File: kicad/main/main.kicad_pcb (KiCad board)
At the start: 2 copper layers, 99.1 x 99.1 mm, 29 parts, among them J1 Barrel_Jack_MountingPin, SW1 Reset, SW2 SW_DIP_x08, U1 GAL16V8, U2 Z80CPU, U3 DS1813-5+, U4 AS6C4008-55PCN, U5 L7805, U6 74HC273, U7 27C512, U8 74HC244, X1 4 MHz

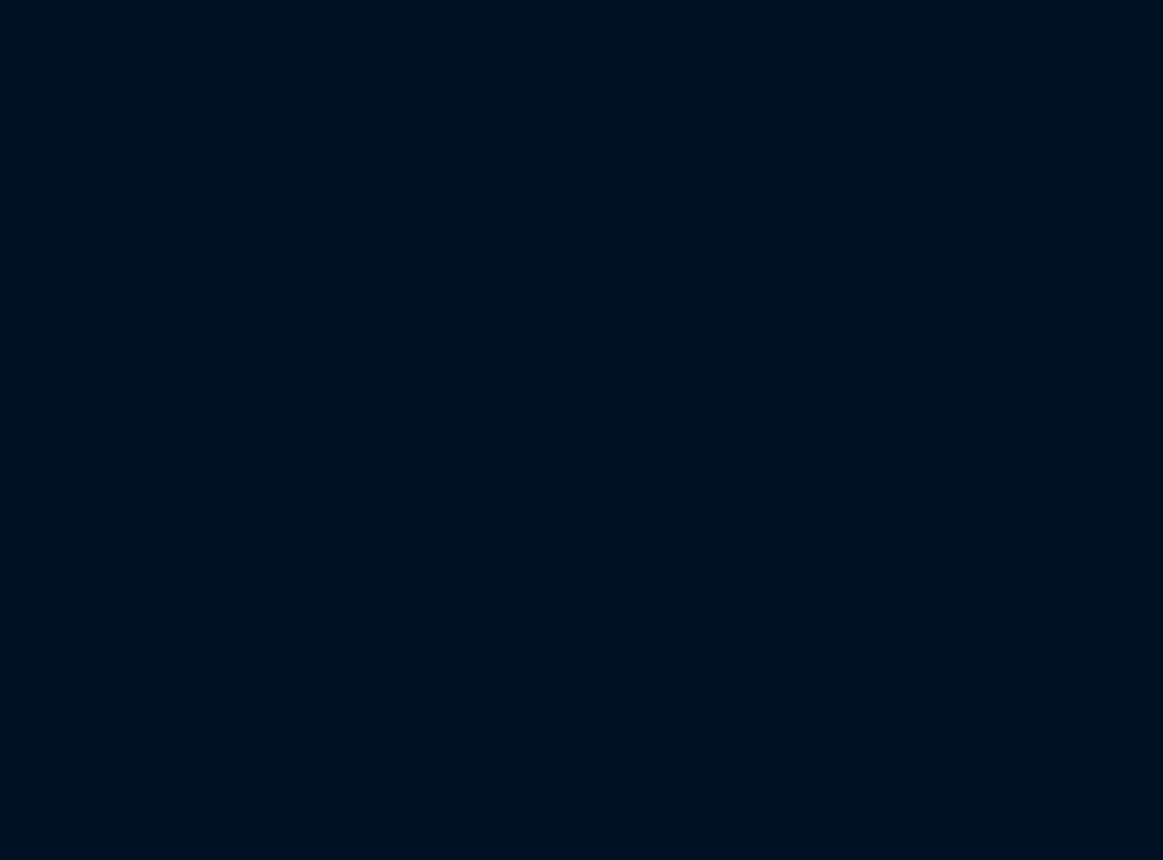
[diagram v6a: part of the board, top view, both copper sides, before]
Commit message: Add new buffers
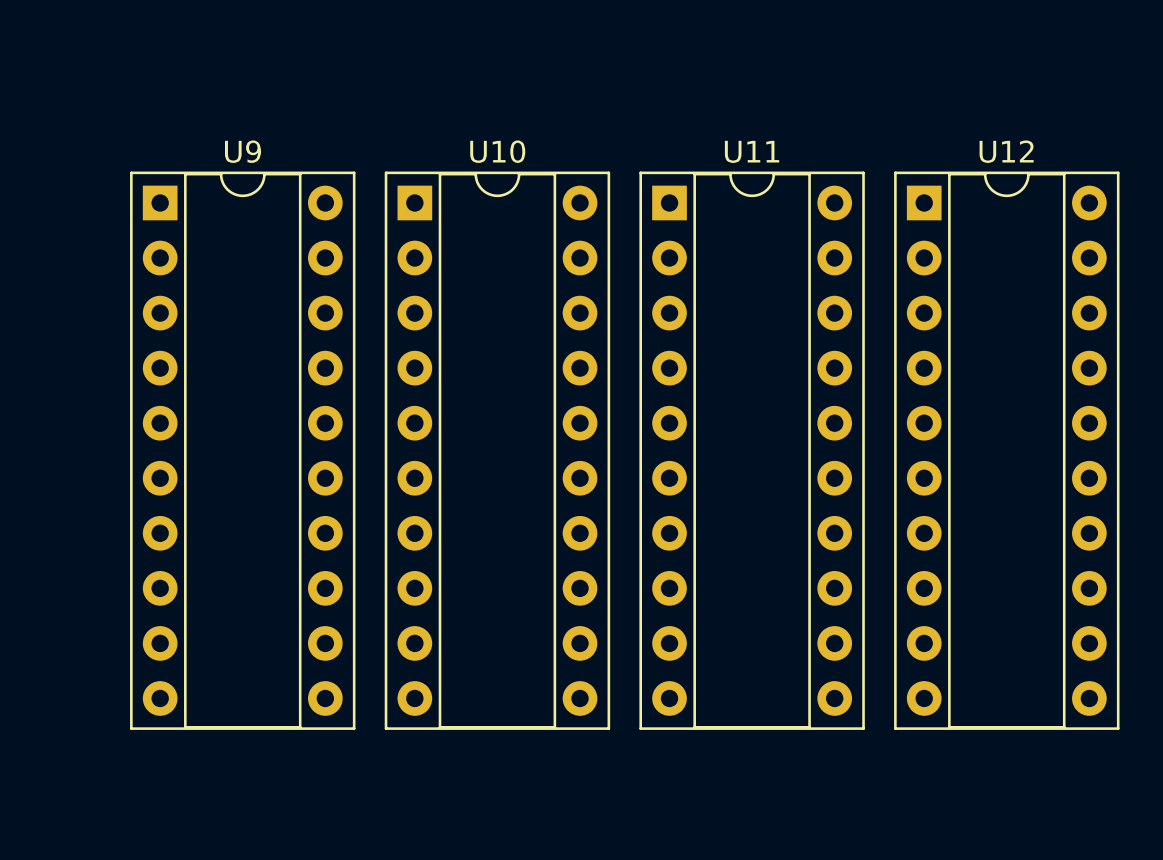
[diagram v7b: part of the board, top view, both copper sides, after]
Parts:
- added U10: 74LS244, Package_DIP:DIP-20_W7.62mm_Socket, F.Cu at (128.9, -66.0)
- added U11: 74LS244, Package_DIP:DIP-20_W7.62mm_Socket, F.Cu at (140.7, -66.0)
- added U12: 74LS244, Package_DIP:DIP-20_W7.62mm_Socket, F.Cu at (152.4, -66.0)
- added U9: 74LS245, Package_DIP:DIP-20_W7.62mm_Socket, F.Cu at (117.2, -66.0)
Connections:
- BAR1 pad 1: Net-(U6-Q0) -> Net-(U6-Q7)
- BAR1 pad 13: Net-(RN2-R8) -> Net-(RN2-R1)
- BAR1 pad 14: Net-(RN2-R7) -> Net-(RN2-R2)
- BAR1 pad 15: Net-(RN2-R6) -> Net-(RN2-R3)
- BAR1 pad 16: Net-(RN2-R5) -> Net-(RN2-R4)
- BAR1 pad 17: Net-(RN2-R4) -> Net-(RN2-R5)
- BAR1 pad 18: Net-(RN2-R3) -> Net-(RN2-R6)
- BAR1 pad 19: Net-(RN2-R2) -> Net-(RN2-R7)
- BAR1 pad 2: Net-(U6-Q1) -> Net-(U6-Q6)
- BAR1 pad 20: Net-(RN2-R1) -> Net-(RN2-R8)
- BAR1 pad 3: Net-(U6-Q2) -> Net-(U6-Q5)
- BAR1 pad 4: Net-(U6-Q3) -> Net-(U6-Q4)
- BAR1 pad 5: Net-(U6-Q4) -> Net-(U6-Q3)
- BAR1 pad 6: Net-(U6-Q5) -> Net-(U6-Q2)
- BAR1 pad 7: Net-(U6-Q6) -> Net-(U6-Q1)
- BAR1 pad 8: Net-(U6-Q7) -> Net-(U6-Q0)
- RN3 pad 1: +5V -> GND
- SW2 pad 1: GND -> +5V
- SW2 pad 10: Net-(RN3-R7) -> Net-(RN3-R2)
- SW2 pad 11: Net-(RN3-R6) -> Net-(RN3-R3)
- SW2 pad 12: Net-(RN3-R5) -> Net-(RN3-R4)
- SW2 pad 13: Net-(RN3-R4) -> Net-(RN3-R5)
- SW2 pad 14: Net-(RN3-R3) -> Net-(RN3-R6)
- SW2 pad 15: Net-(RN3-R2) -> Net-(RN3-R7)
- SW2 pad 16: Net-(RN3-R1) -> Net-(RN3-R8)
- SW2 pad 2: GND -> +5V
- SW2 pad 3: GND -> +5V
- SW2 pad 4: GND -> +5V
- SW2 pad 5: GND -> +5V
- SW2 pad 6: GND -> +5V
- SW2 pad 7: GND -> +5V
- SW2 pad 8: GND -> +5V
- SW2 pad 9: Net-(RN3-R8) -> Net-(RN3-R1)
- U2 pad 1: A_{11} -> /A^{u}_{11}
- U2 pad 10: D_{6} -> /D^{u}_{6}
- U2 pad 12: D_{2} -> /D^{u}_{2}
- U2 pad 13: D_{7} -> /D^{u}_{7}
- U2 pad 14: D_{0} -> /D^{u}_{0}
- U2 pad 15: D_{1} -> /D^{u}_{1}
- U2 pad 2: A_{12} -> /A^{u}_{12}
- U2 pad 21: ~{RD} -> ~{RD^{u}}
- U2 pad 22: ~{WD} -> ~{WD^{u}}
- U2 pad 3: A_{13} -> /A^{u}_{13}
- U2 pad 30: A_{0} -> /A^{u}_{0}
- U2 pad 31: A_{1} -> /A^{u}_{1}
- U2 pad 32: A_{2} -> /A^{u}_{2}
- U2 pad 33: A_{3} -> /A^{u}_{3}
- U2 pad 34: A_{4} -> /A^{u}_{4}
- U2 pad 35: A_{5} -> /A^{u}_{5}
- U2 pad 36: A_{6} -> /A^{u}_{6}
- U2 pad 37: A_{7} -> /A^{u}_{7}
- U2 pad 38: A_{8} -> /A^{u}_{8}
- U2 pad 39: A_{9} -> /A^{u}_{9}
- U2 pad 4: A_{14} -> /A^{u}_{14}
- U2 pad 40: A_{10} -> /A^{u}_{10}
- U2 pad 5: A_{15} -> /A^{u}_{15}
- U2 pad 7: D_{4} -> /D^{u}_{4}
- U2 pad 8: D_{3} -> /D^{u}_{3}
- U2 pad 9: D_{5} -> /D^{u}_{5}
